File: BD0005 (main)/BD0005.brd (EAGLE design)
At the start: 67.3 x 33 mm, 67 parts, among them J1 CONN_MICROUSB_FEMALE, J2 HEADER_1X3, J3 HEADER_1X3FEMALE, J4 HEADER_1X3FEMALE, U2 REG_AP2114H-3.3TRG1, U3 SAMD21E__A-MU_16(64K), X1 XTAL_MC-146-32.7680JKA-A0:ROHS

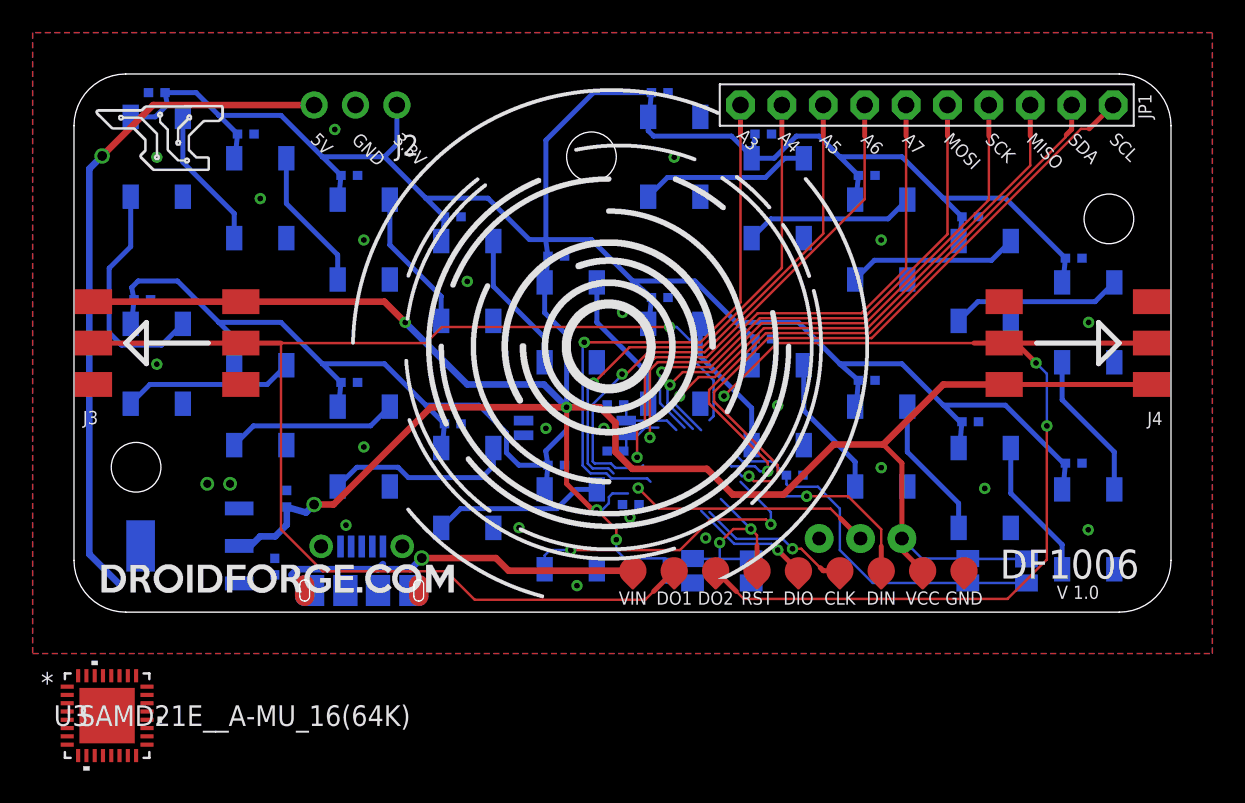
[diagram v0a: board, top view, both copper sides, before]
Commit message: Placed new microcontroller on pcb
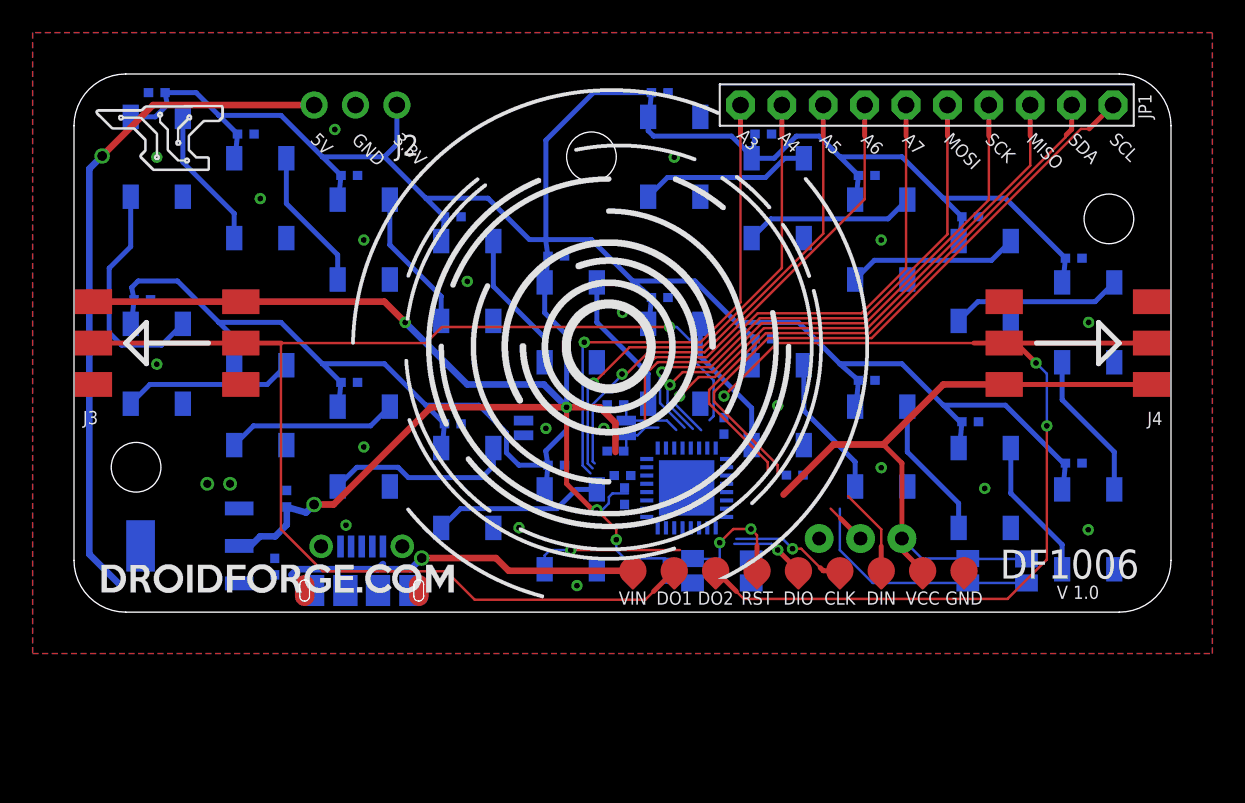
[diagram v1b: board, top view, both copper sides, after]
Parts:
- added C26, C27: 0.1uF, DroidForge:0402
- moved U3 38.2 mm to (37.6, 7.62), flipped to the bottom, turned to 270 degrees
- moved C3 1.85 mm to (33.7, 8.38)
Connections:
- removed net A10: U3.13
- removed net A11: U3.14
- removed net A16: U3.17
- removed net A17: U3.18
- removed net A18: U3.19
- removed net A19: U3.20
- removed net A22: U3.21
- removed net A24: U3.23
- removed net A25: U3.24
- removed net A30: U3.31
- removed net A31: U3.32
- removed net A8: U3.11
- removed net A9: U3.12
- removed net VDDANA: U3.9
- removed net VDDCORE: U3.29
- removed net VDDIN: U3.30
- new net N$2: C3.P$1, U3.30
- new net N$3: C26.P$1, U3.9
- new net N$6: C27.P$1, U3.29
- net BIN: now also U3.14
- net D+: now also U3.24
- net D-: now also U3.23
- net DIN: now also U3.11
- net DOUT_1: now also U3.12
- net DOUT_2: now also U3.13
- net GND: now also C26.P$2, C27.P$2, C3.P$2
- net MISO: now also U3.21
- net MOSI: now also U3.19
- net RESET: now also U3.26
- net SCK: now also U3.20
- net SCL: now also U3.18
- net SDA: now also U3.17
- net SWCLK: now also U3.31
- net SWDIO: now also U3.32
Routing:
- net DIN: track 30.3 -> 14.7 mm, vias 3 -> 1
- net A2: track 15.1 -> 2.59 mm, vias 1 -> 0
- net VCC: track 340.8 -> 329.4 mm
- net BIN: track 22.7 -> 14.9 mm
- net RESET: track 14.6 -> 7.95 mm
- net A7: track 32.7 -> 28.3 mm, vias 1 -> 0
- net A3: track 34.9 -> 31.0 mm
- net A5: track 33.2 -> 30.1 mm
- net SWDIO: track 7.49 -> 4.62 mm
- net SCL: track 41.2 -> 38.5 mm, vias 1 -> 0
- net SDA: track 39.4 -> 36.9 mm, vias 1 -> 0
- net A6: track 29.3 -> 26.9 mm, vias 1 -> 0
- net SWCLK: track 9.49 -> 7.16 mm
- net A4: track 31.4 -> 30.0 mm

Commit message: Finished rerouting board for new SAMD21E processor. Also added VCC connection to processor on schematic
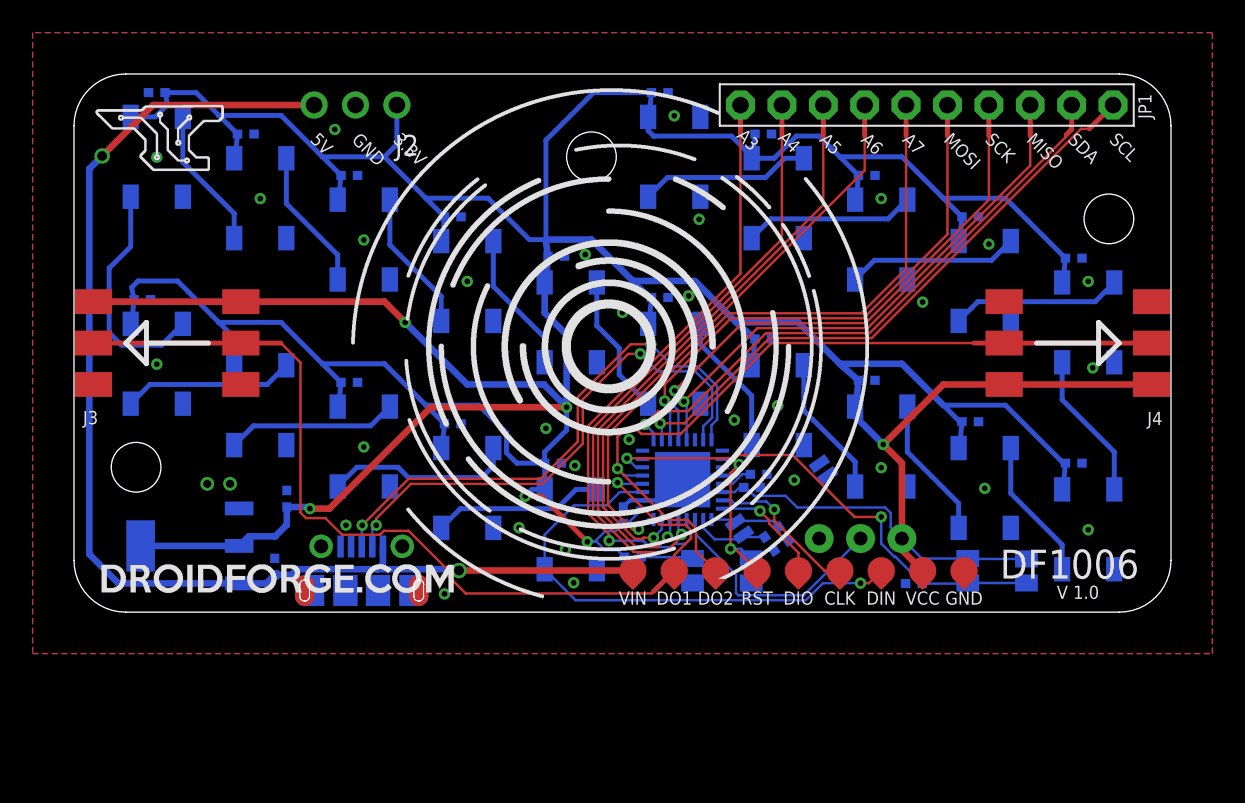
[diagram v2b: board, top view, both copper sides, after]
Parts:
- moved X1 13.4 mm to (43.4, 6.93), turned to 145 degrees
- moved C5 12.7 mm to (42.7, 4.19), turned to 235 degrees
- moved C4 11.5 mm to (43.5, 4.80), turned to 235 degrees
- moved R3 9.89 mm to (51.5, 1.75), turned to 180 degrees
- moved C27 8.34 mm to (42.0, 8.46), turned to 180 degrees
- moved C26 8.26 mm to (33.7, 5.94)
- moved C3 7.98 mm to (41.6, 7.65), turned to 180 degrees
- moved R1 2.27 mm to (34.3, 3.38), turned to 0 degrees
- moved U3 0.57 mm to (37.3, 8.13), turned to 90 degrees
- moved C6 0.24 mm to (29.4, 9.14)
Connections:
- removed net N$2: C3.P$1, U3.30
- removed net N$3: C26.P$1, U3.9
- net VCC: now also C26.P$1, C3.P$1, U3.30, U3.9
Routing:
- net D+: track 0.00 -> 33.8 mm, vias 0 -> 2
- net D-: track 0.00 -> 32.5 mm, vias 0 -> 2
- net DOUT_1: track 81.0 -> 58.6 mm
- net DIN: track 14.7 -> 31.4 mm
- net DOUT_2: track 75.6 -> 60.1 mm, vias 3 -> 1
- net BIN: track 14.9 -> 30.0 mm, vias 0 -> 2
- net A7: track 28.3 -> 40.5 mm, vias 0 -> 1
- net A2: track 2.59 -> 14.7 mm
- net VIN: track 63.7 -> 75.1 mm
- net A6: track 26.9 -> 36.6 mm, vias 0 -> 1
- net A4: track 30.0 -> 37.7 mm
- net VCC: track 329.4 -> 336.4 mm, vias 5 -> 6
- net A5: track 30.1 -> 37.1 mm
- net GND: track 0.00 -> 6.88 mm, vias 22 -> 33
- net A3: track 31.0 -> 37.8 mm
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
